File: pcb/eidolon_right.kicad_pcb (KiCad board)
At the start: 2 copper layers, 117.1 x 83.9 mm, 37 parts

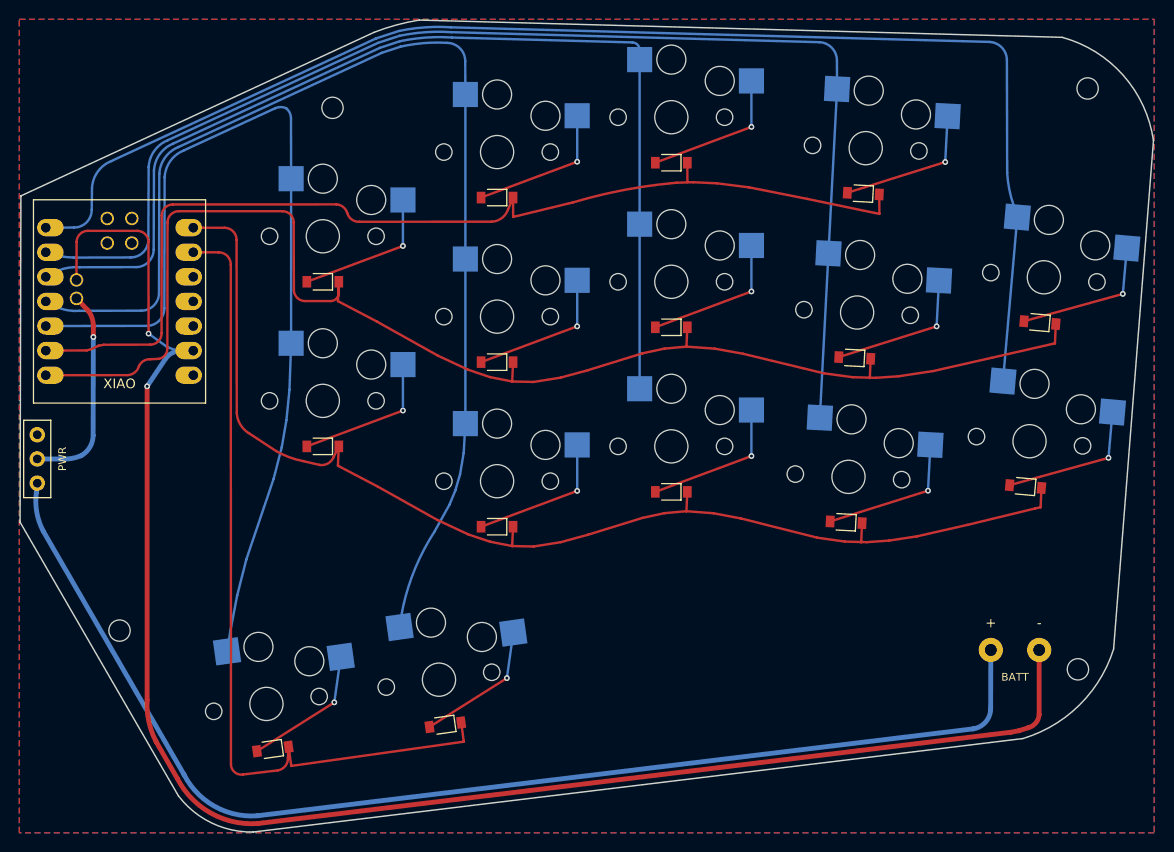
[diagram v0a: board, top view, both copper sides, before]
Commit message: fix(pcb): land faithfully re-routed boards + gerbers (corrected pinout)
Replace the old buggy routed boards with the re-routed eidolon_{left,right}
from the phantom autorouter (~/git/phantom-router), built on the corrected
XIAO right-column pinout. Both halves: 0 DRC violations, 0 unconnected.

Whole-module GND pour keepout; explicit hand-shaped B.Cu GND margin rail;
R2/R3 re-derived for the moved pinout (rail crossings on F.Cu, minimal vias);
the mirrored right half's forced GND/RAW crossing and under-MCU access-pad
jumper threaded with one via each. Re-exported gerbers (all layers + drill).

Fab-ready.

Co-Authored-By: Claude Opus 4.8 <noreply@anthropic.com>
Claude-Session: https://claude.ai/code/session_01MD1mhgQXFf8iwVCJGWMS4x
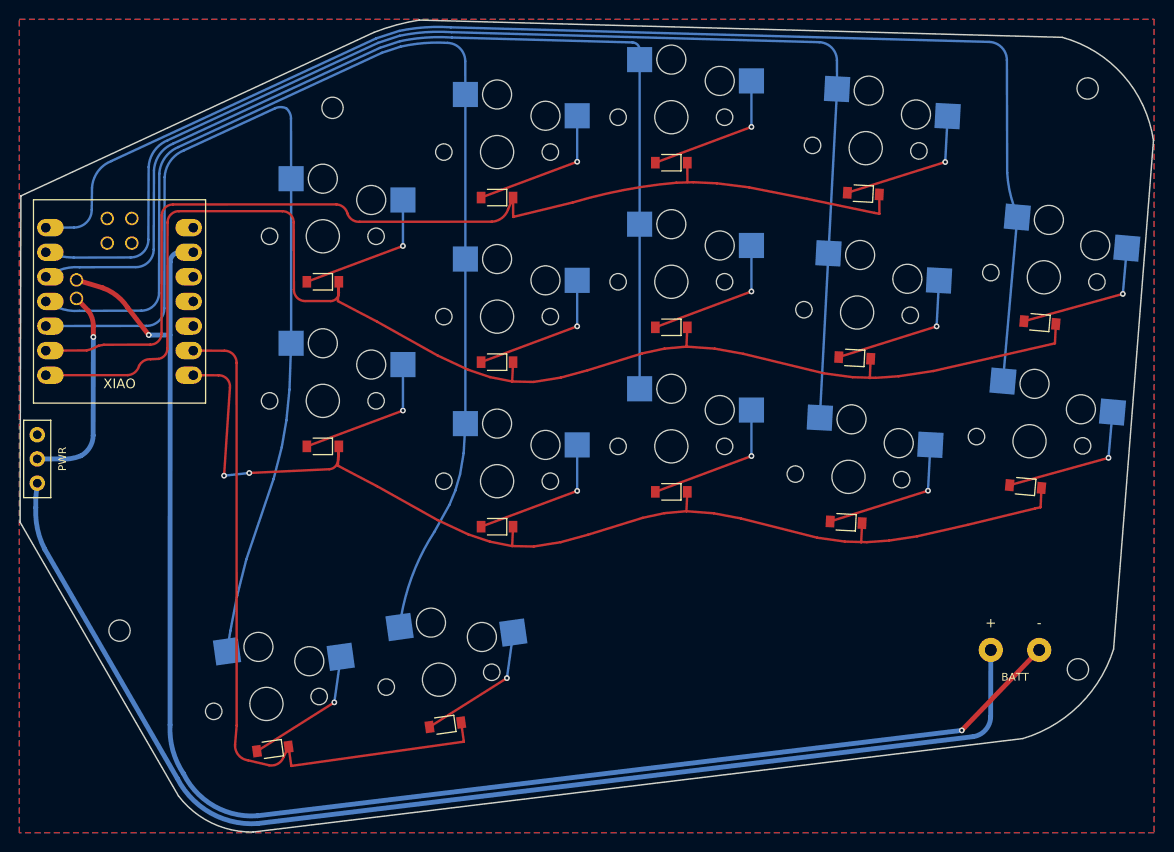
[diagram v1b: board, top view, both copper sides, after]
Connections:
- MCU1 pad 10: P3V3 -> D9
- MCU1 pad 12: D9 -> P3V3
- MCU1 pad 13: R3 -> GND
- MCU1 pad 14: R2 -> P5V
- MCU1 pad 8: P5V -> R2
- MCU1 pad 9: GND -> R3
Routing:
- net R3: track 86.5 -> 74.1 mm
- net GND: track 173.6 -> 162.0 mm
- net R2: track 122.3 -> 113.0 mm, vias 0 -> 2
- net RAW_BATT: track 126.7 -> 128.5 mm

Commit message: feat(pcb): per-half XIAO pin maps; declutter right-half routing
Each half is an independent wireless unit, so the net->pin maps need not match.
Give the right half its own map (all 4 rows on the matrix-facing D7-D10 edge:
D7:R3 D8:R2 D9:R1 D10:R0; columns on D0-D4). The left keeps R0/R1 on D5/D6.

This moves R0/R1 off the far MCU edge on the right, so they fan out directly
east instead of crossing back over the MCU ("west-about" boxed routes). Only
the 5 columns now cross under the MCU on the right (the physical floor). Both
halves re-routed to 0 DRC / 0 unconnected; gerbers re-exported.

FIRMWARE: the halves now use different MATRIX_ROW_PINS (left D5-D8, right
D7-D10) -- update each half's kscan/matrix map accordingly.

Co-Authored-By: Claude Opus 4.8 <noreply@anthropic.com>
Claude-Session: https://claude.ai/code/session_01MD1mhgQXFf8iwVCJGWMS4x
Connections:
- MCU1 pad 10: D9 -> R1
- MCU1 pad 11: D10 -> R0
- MCU1 pad 6: R0 -> D5
- MCU1 pad 7: R1 -> D6
- MCU1 pad 8: R2 -> R3
- MCU1 pad 9: R3 -> R2
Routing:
- net R1: track 142.0 -> 104.6 mm
- net R0: track 108.4 -> 82.5 mm, vias 0 -> 2
- net R3: track 74.1 -> 70.8 mm
- net R2: track 113.0 -> 111.2 mm, vias 2 -> 0
